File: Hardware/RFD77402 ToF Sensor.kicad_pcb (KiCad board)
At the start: 2 copper layers, 25.4 x 25.4 mm, 18 parts, among them J1 Qwiic_Connector, J2 Qwiic_Connector, J3 CONN_01X01, J4 I2C_Standard_PTH_Connector, U1 RFD77402, U2 SPARKX-LOGO4, U3 SPARKX-LOGO4, U4 CC_LICENSE

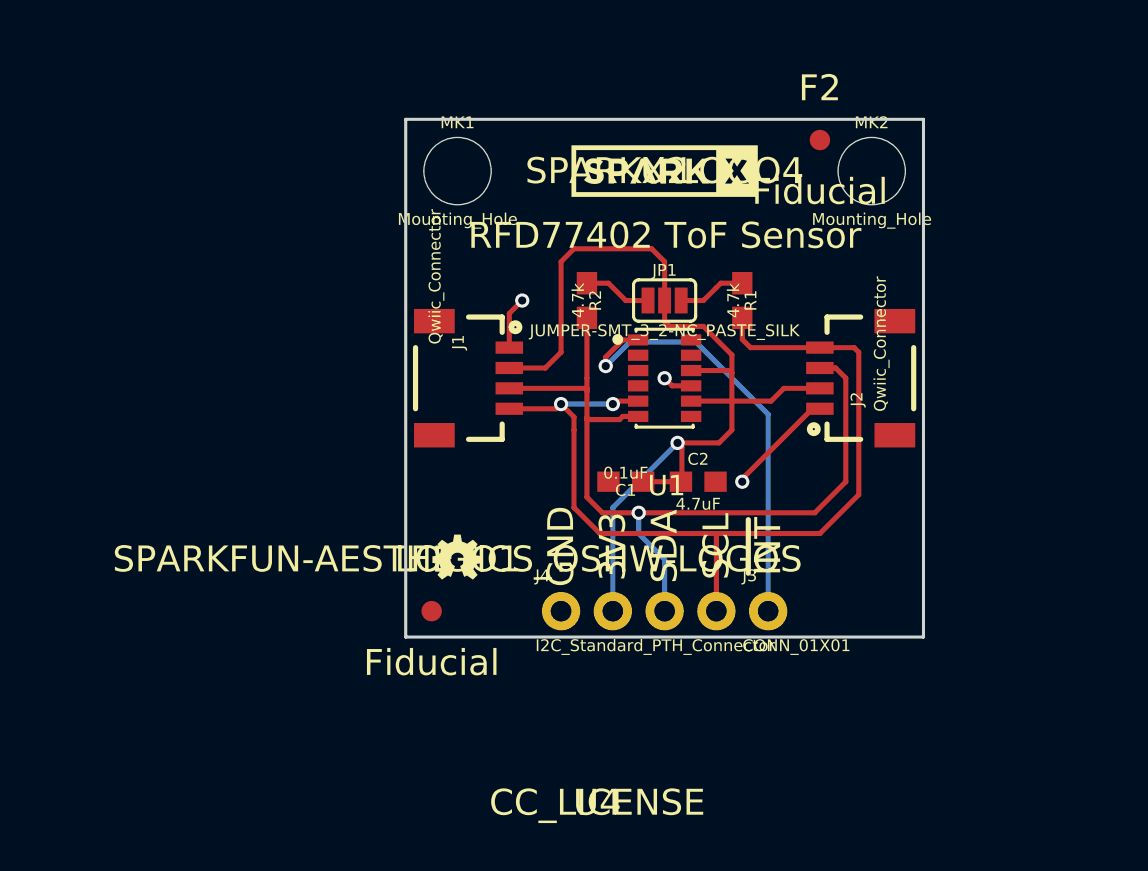
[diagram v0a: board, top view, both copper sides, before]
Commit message: Decreasing paste on sensor
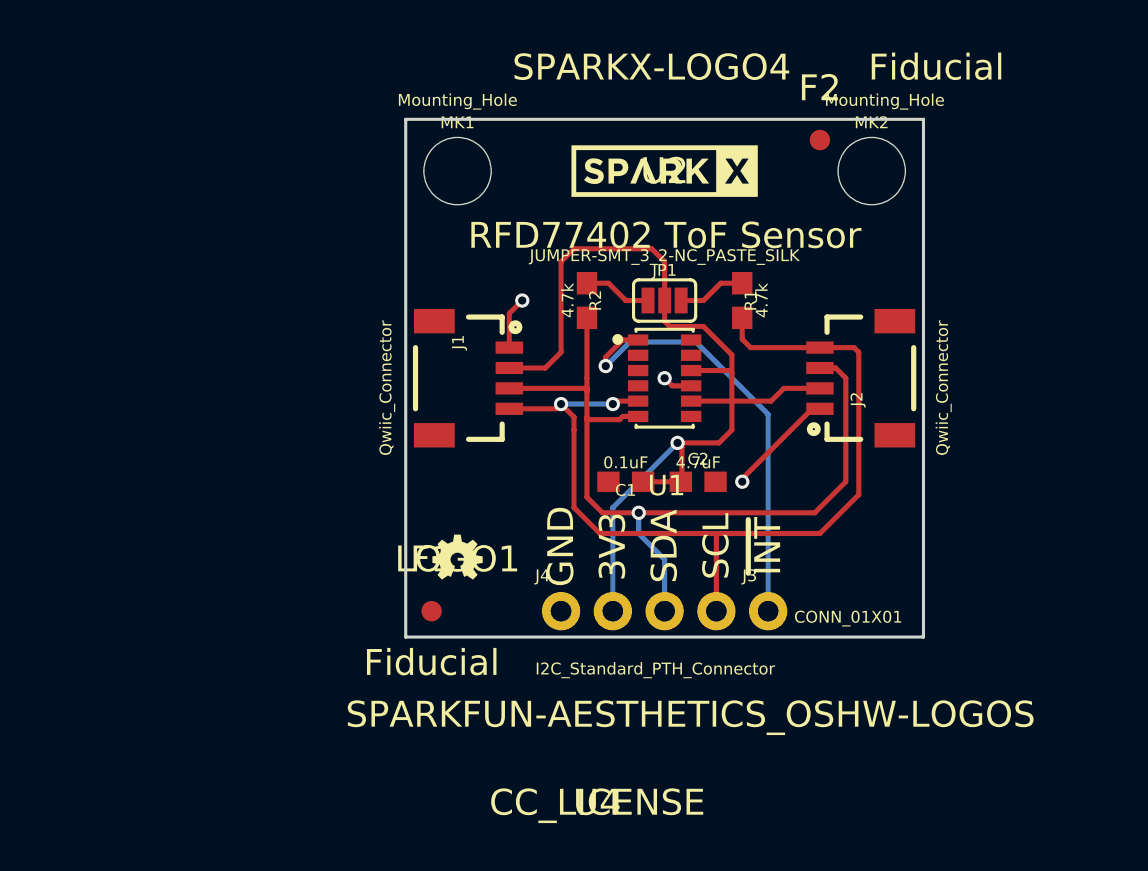
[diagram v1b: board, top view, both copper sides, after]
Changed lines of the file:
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@@
     (links 24)
     (no_connects 0)
-    (area 117.656001 88.5742 163.350007 126.4622)
+    (area 129.086001 85.6532 173.174 126.4622)
     (thickness 1.6)
     (drawings 16)
@@
     (nets 8)
   )
-  (page A4)
+  (page USLetter)
   (layers
-    (0 F.Cu signal)
-    (31 B.Cu signal)
+    (0 F.Cu signal hide)
+    (31 B.Cu signal hide)
     (34 B.Paste user hide)
     (35 F.Paste user)
-    (36 B.SilkS user)
+    (36 B.SilkS user hide)
     (37 F.SilkS user)
     (38 B.Mask user)
-    (39 F.Mask user)
+    (39 F.Mask user hide)
     (44 Edge.Cuts user)
     (46 B.CrtYd user hide)
@@
     (pad_to_mask_clearance 0.075)
     (aux_axis_origin 0 0)
-    (visible_elements 7FFCF3E9)
+    (visible_elements 7FFDF3E9)
     (pcbplotparams
       (layerselection 0x00030_80000001)
@@
       (effects (font (size 0.57912 0.57912) (thickness 0.12192)) (justify bottom))
     )
-    (fp_text value JUMPER-SMT_3_2-NC_PASTE_SILK (at 0 1.143) (layer F.SilkS)
+    (fp_text value JUMPER-SMT_3_2-NC_PASTE_SILK (at 0 -2.54) (layer F.SilkS)
       (effects (font (size 0.57912 0.57912) (thickness 0.12192)) (justify top))
     )
@@
       (effects (font (size 0.57912 0.57912) (thickness 0.12192)) (justify left bottom))
     )
-    (fp_text value Qwiic_Connector (at -1.651 3.302 270) (layer F.SilkS)
+    (fp_text value Qwiic_Connector (at 3.81 5.715 270) (layer F.SilkS)
       (effects (font (size 0.57912 0.57912) (thickness 0.12192)) (justify left bottom))
     )
@@
       (effects (font (size 0.57912 0.57912) (thickness 0.12192)) (justify left bottom))
     )
-    (fp_text value Qwiic_Connector (at -1.651 3.302 90) (layer F.SilkS)
+    (fp_text value Qwiic_Connector (at -3.81 6.35 90) (layer F.SilkS)
       (effects (font (size 0.57912 0.57912) (thickness 0.12192)) (justify left bottom))
     )
@@
       (effects (font (size 0.57912 0.57912) (thickness 0.12192)) (justify left bottom))
     )
-    (fp_text value CONN_01X01 (at -1.27 2.032) (layer F.SilkS)
+    (fp_text value CONN_01X01 (at 1.27 0.635) (layer F.SilkS)
       (effects (font (size 0.57912 0.57912) (thickness 0.12192)) (justify left bottom))
     )
@@
       (effects (font (size 0.57912 0.57912) (thickness 0.12192)) (justify left bottom))
     )
-    (fp_text value I2C_Standard_PTH_Connector (at -1.27 2.032) (layer F.SilkS)
+    (fp_text value I2C_Standard_PTH_Connector (at -1.27 3.175) (layer F.SilkS)
       (effects (font (size 0.57912 0.57912) (thickness 0.12192)) (justify left bottom))
     )
@@
       (effects (font (thickness 0.15)) (justify mirror))
     )
-    (fp_text value SPARKX-LOGO4 (at 0 -2.54 180) (layer B.SilkS)
+    (fp_text value SPARKX-LOGO4 (at 0 6.985 180) (layer B.SilkS)
       (effects (font (thickness 0.15)) (justify mirror))
     )
@@
       (effects (font (size 0.57912 0.57912) (thickness 0.12192)) (justify bottom))
     )
-    (fp_text value 0.1uF (at 0 0.762 180) (layer F.SilkS)
+    (fp_text value 0.1uF (at 0 1.27 180) (layer F.SilkS)
       (effects (font (size 0.57912 0.57912) (thickness 0.12192)) (justify top))
     )
@@
       (effects (font (thickness 0.15)))
     )
-    (fp_text value SPARKFUN-AESTHETICS_OSHW-LOGOS (at 0 0) (layer F.SilkS)
+    (fp_text value SPARKFUN-AESTHETICS_OSHW-LOGOS (at 11.43 7.62) (layer F.SilkS)
       (effects (font (thickness 0.15)))
     )
@@
       (effects (font (size 0.57912 0.57912) (thickness 0.12192)) (justify bottom))
     )
-    (fp_text value Mounting_Hole (at 0 2.032) (layer F.SilkS)
+    (fp_text value Mounting_Hole (at 0 -3.81) (layer F.SilkS)
       (effects (font (size 0.57912 0.57912) (thickness 0.12192)) (justify top))
     )
@@
       (effects (font (size 0.57912 0.57912) (thickness 0.12192)) (justify bottom))
     )
-    (fp_text value Mounting_Hole (at 0 2.032) (layer F.SilkS)
+    (fp_text value Mounting_Hole (at 0.635 -3.81) (layer F.SilkS)
       (effects (font (size 0.57912 0.57912) (thickness 0.12192)) (justify top))
     )
@@
       (effects (font (size 0.57912 0.57912) (thickness 0.12192)) (justify bottom))
     )
-    (fp_text value 4.7k (at 0 0.762 270) (layer F.SilkS)
+    (fp_text value 4.7k (at 0 -0.635 270) (layer F.SilkS)
       (effects (font (size 0.57912 0.57912) (thickness 0.12192)) (justify top))
     )
@@
       (effects (font (size 0.57912 0.57912) (thickness 0.12192)) (justify bottom))
     )
-    (fp_text value 4.7k (at 0 0.762 270) (layer F.SilkS)
+    (fp_text value 4.7k (at 0 1.27 270) (layer F.SilkS)
       (effects (font (size 0.57912 0.57912) (thickness 0.12192)) (justify top))
     )
@@
   (module SparkFun_Kicad-Sensors:RFD77402 (layer F.Cu)
     (at 149.86 104.14)
+    (solder_paste_ratio -0.15)
     (fp_text reference U1 (at 0.1 5.28) (layer F.SilkS)
       (effects (font (size 1 1) (thickness 0.15)))
     )
-    (fp_text value RFD77402 (at 0.1 -4.88) (layer F.Fab)
+    (fp_text value RFD77402 (at 0 1.27) (layer F.Fab)
       (effects (font (size 1 1) (thickness 0.15)))
     )
@@
       (effects (font (size 0.57912 0.57912) (thickness 0.12192)) (justify bottom))
     )
-    (fp_text value 4.7uF (at 0 0.762) (layer F.SilkS)
+    (fp_text value 4.7uF (at 0 -1.27) (layer F.SilkS)
       (effects (font (size 0.57912 0.57912) (thickness 0.12192)) (justify top))
     )
@@
       (effects (font (thickness 0.15)))
     )
-    (fp_text value SPARKX-LOGO4 (at 0 0) (layer F.SilkS)
+    (fp_text value SPARKX-LOGO4 (at -0.635 -5.08) (layer F.SilkS)
       (effects (font (thickness 0.15)))
     )
@@
       (effects (font (thickness 0.15)))
     )
-    (fp_text value Fiducial (at 0 2.54) (layer F.SilkS)
-      (effects (font (thickness 0.15)))
-    )
+    (fp_text value Fiducial (at 5.715 -3.556) (layer F.SilkS)
+      (effects (font (thickness 0.15)))
+    )
